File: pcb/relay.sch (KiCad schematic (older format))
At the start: 22 parts, among them IC1 ATTINY13-P, P1 CONN_01X02, P2 CONN_02X20, Q1 BC548, Q2 BC548, SW1 SW_PUSH, U1 78L05, U2 DX_MODULE

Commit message: More work on PCB
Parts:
- removed U1: 78L05, symbol 78L05
- added U1: MC78L05ACP, TO_SOT_Packages_THT:TO-92_Rugged, symbol MC78L05ACP
- C1: footprint (none) -> Capacitors_ThroughHole:C_Disc_D6_P5
- C2, C3: footprint (none) -> Capacitors_ThroughHole:C_Radial_D5_L11_P2.5
- D1: footprint (none) -> LEDs:LED-5MM
- D2, D3: footprint (none) -> Discret:D5
- IC1: footprint DIP8 -> Housings_DIP:DIP-8_W7.62mm_LongPads
- JP1: footprint (none) -> Pin_Headers:Pin_Header_Straight_1x02
- P1: footprint (none) -> Connect:bornier2
- P2: footprint (none) -> Connect:IDC_Header_Straight_40pins
- Q1, Q2: footprint TO-92 -> TO_SOT_Packages_THT:TO-92_Rugged
- R1, R2, R3, R4, R5: footprint (none) -> Resistors_ThroughHole:Resistor_Horizontal_RM10mm
- RL1, RL2: footprint (none) -> anritsu:anritsu
- SW1: footprint (none) -> Buttons_Switches_ThroughHole:SW_PUSH-12mm
- U2: footprint (none) -> dx_module:dx_module
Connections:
- net +12V: now also C2.1, P1.2 (P2), U1.3 (IN)
- net +5VD: now also U1.1 (OUT)
- net at C2.2, C3.2, P1.1 (P1): now also U1.2 (GND)
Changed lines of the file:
@@
 LIBS:anritsu
 LIBS:dx_module
+LIBS:relay-cache
 EELAYER 25 0
 EELAYER END
@@
 F 0 "IC1" H 1150 1850 50  0000 C CNN
 F 1 "ATTINY13-P" H 2600 1050 50  0000 C CNN
-F 2 "DIP8" H 2600 1450 50  0000 C CIN
+F 2 "Housings_DIP:DIP-8_W7.62mm_LongPads" H 2600 1450 50  0000 C CIN
 F 3 "" H 1150 1800 50  0000 C CNN
 	1    1950 1450
@@
 F 0 "Q1" H 5450 2025 50  0000 L CNN
 F 1 "BC548" H 5450 1950 50  0000 L CNN
-F 2 "TO-92" H 5450 1875 50  0000 L CIN
+F 2 "TO_SOT_Packages_THT:TO-92_Rugged" H 5450 1875 50  0000 L CIN
 F 3 "" H 5250 1950 50  0000 L CNN
 	1    5250 1950
@@
 F 0 "Q2" H 5450 4175 50  0000 L CNN
 F 1 "BC548" H 5450 4100 50  0000 L CNN
-F 2 "TO-92" H 5450 4025 50  0000 L CIN
+F 2 "TO_SOT_Packages_THT:TO-92_Rugged" H 5450 4025 50  0000 L CIN
 F 3 "" H 5250 4100 50  0000 L CNN
 	1    5250 4100
@@
 $EndComp
 $Comp
-L GNDD #PWR?
+L GNDD #PWR01
 U 1 1 57CD5BEB
 P 5350 2250
-F 0 "#PWR?" H 5350 2000 50  0001 C CNN
+F 0 "#PWR01" H 5350 2000 50  0001 C CNN
 F 1 "GNDD" H 5350 2100 50  0000 C CNN
 F 2 "" H 5350 2250 50  0000 C CNN
@@
 $EndComp
 $Comp
-L GNDD #PWR?
+L GNDD #PWR02
 U 1 1 57CD5C09
 P 950 1200
-F 0 "#PWR?" H 950 950 50  0001 C CNN
+F 0 "#PWR02" H 950 950 50  0001 C CNN
 F 1 "GNDD" H 950 1050 50  0000 C CNN
 F 2 "" H 950 1200 50  0000 C CNN
@@
 $EndComp
 $Comp
-L +5VD #PWR?
+L +5VD #PWR03
 U 1 1 57CD5C27
 P 950 1700
-F 0 "#PWR?" H 950 1550 50  0001 C CNN
+F 0 "#PWR03" H 950 1550 50  0001 C CNN
 F 1 "+5VD" H 950 1840 50  0000 C CNN
 F 2 "" H 950 1700 50  0000 C CNN
@@
 F 0 "D2" H 5350 1350 50  0000 C CNN
 F 1 "D" H 5350 1150 50  0000 C CNN
-F 2 "" H 5350 1250 50  0000 C CNN
+F 2 "Discret:D5" H 5350 1250 50  0000 C CNN
 F 3 "" H 5350 1250 50  0000 C CNN
 	1    5350 1250
@@
 F 0 "D3" H 5350 3450 50  0000 C CNN
 F 1 "D" H 5350 3250 50  0000 C CNN
-F 2 "" H 5350 3350 50  0000 C CNN
+F 2 "Discret:D5" H 5350 3350 50  0000 C CNN
 F 3 "" H 5350 3350 50  0000 C CNN
 	1    5350 3350
@@
 F 0 "R4" V 4980 1600 50  0000 C CNN
 F 1 "5K6" V 4900 1600 50  0000 C CNN
-F 2 "" V 4830 1600 50  0000 C CNN
+F 2 "Resistors_ThroughHole:Resistor_Horizontal_RM10mm" V 4830 1600 50  0000 C CNN
 F 3 "" H 4900 1600 50  0000 C CNN
 	1    4900 1600
@@
 F 0 "R5" V 4880 3500 50  0000 C CNN
 F 1 "5K6" V 4800 3500 50  0000 C CNN
-F 2 "" V 4730 3500 50  0000 C CNN
+F 2 "Resistors_ThroughHole:Resistor_Horizontal_RM10mm" V 4730 3500 50  0000 C CNN
 F 3 "" H 4800 3500 50  0000 C CNN
 	1    4800 3500
@@
 F 0 "R2" V 4530 1850 50  0000 C CNN
 F 1 "1M" V 4450 1850 50  0000 C CNN
-F 2 "" V 4380 1850 50  0000 C CNN
+F 2 "Resistors_ThroughHole:Resistor_Horizontal_RM10mm" V 4380 1850 50  0000 C CNN
 F 3 "" H 4450 1850 50  0000 C CNN
 	1    4450 1850
@@
 F 0 "R3" V 4530 2250 50  0000 C CNN
 F 1 "330K" V 4450 2250 50  0000 C CNN
-F 2 "" V 4380 2250 50  0000 C CNN
+F 2 "Resistors_ThroughHole:Resistor_Horizontal_RM10mm" V 4380 2250 50  0000 C CNN
 F 3 "" H 4450 2250 50  0000 C CNN
 	1    4450 2250
@@
 $EndComp
 $Comp
-L +12V #PWR?
+L +12V #PWR04
 U 1 1 57CD66EF
 P 4450 1700
-F 0 "#PWR?" H 4450 1550 50  0001 C CNN
+F 0 "#PWR04" H 4450 1550 50  0001 C CNN
 F 1 "+12V" H 4450 1840 50  0000 C CNN
 F 2 "" H 4450 1700 50  0000 C CNN
@@
 F 0 "C1" H 4225 2350 50  0000 L CNN
 F 1 "C" H 4225 2150 50  0000 L CNN
-F 2 "" H 4238 2100 50  0000 C CNN
+F 2 "Capacitors_ThroughHole:C_Disc_D6_P5" H 4238 2100 50  0000 C CNN
 F 3 "" H 4200 2250 50  0000 C CNN
 	1    4200 2250
@@
 $EndComp
 $Comp
-L GNDD #PWR?
+L GNDD #PWR05
 U 1 1 57CD68E3
 P 4450 2500
-F 0 "#PWR?" H 4450 2250 50  0001 C CNN
+F 0 "#PWR05" H 4450 2250 50  0001 C CNN
 F 1 "GNDD" H 4450 2350 50  0000 C CNN
 F 2 "" H 4450 2500 50  0000 C CNN
@@
 F 0 "P1" H 1250 5150 50  0000 C CNN
 F 1 "CONN_01X02" V 1350 5000 50  0000 C CNN
-F 2 "" H 1250 5000 50  0000 C CNN
+F 2 "Connect:bornier2" H 1250 5000 50  0000 C CNN
 F 3 "" H 1250 5000 50  0000 C CNN
 	1    1250 5000
@@
 F 0 "C2" H 2275 5300 50  0000 L CNN
 F 1 "1uF" H 2275 5100 50  0000 L CNN
-F 2 "" H 2288 5050 50  0000 C CNN
+F 2 "Capacitors_ThroughHole:C_Radial_D5_L11_P2.5" H 2288 5050 50  0000 C CNN
 F 3 "" H 2250 5200 50  0000 C CNN
 	1    2250 5200
@@
 F 0 "C3" H 3375 5300 50  0000 L CNN
 F 1 "1uF" H 3375 5100 50  0000 L CNN
-F 2 "" H 3388 5050 50  0000 C CNN
+F 2 "Capacitors_ThroughHole:C_Radial_D5_L11_P2.5" H 3388 5050 50  0000 C CNN
 F 3 "" H 3350 5200 50  0000 C CNN
 	1    3350 5200
@@
 $EndComp
 $Comp
-L 78L05 U1
-U 1 1 57CD72E7
-P 2850 5000
-F 0 "U1" H 3000 4804 50  0000 C CNN
-F 1 "78L05" H 2850 5200 50  0000 C CNN
-F 2 "" H 2850 5000 50  0000 C CNN
-F 3 "" H 2850 5000 50  0000 C CNN
-	1    2850 5000
-	1    0    0    -1
-$EndComp
-$Comp
-L +5VD #PWR?
+L +5VD #PWR06
 U 1 1 57CD74DA
 P 3350 4950
-F 0 "#PWR?" H 3350 4800 50  0001 C CNN
+F 0 "#PWR06" H 3350 4800 50  0001 C CNN
 F 1 "+5VD" H 3350 5090 50  0000 C CNN
 F 2 "" H 3350 4950 50  0000 C CNN
@@
 $EndComp
 $Comp
-L +12V #PWR?
+L +12V #PWR07
 U 1 1 57CD7D1E
-P 1650 4950
-F 0 "#PWR?" H 1650 4800 50  0001 C CNN
-F 1 "+12V" H 1650 5090 50  0000 C CNN
-F 2 "" H 1650 4950 50  0000 C CNN
-F 3 "" H 1650 4950 50  0000 C CNN
-	1    1650 4950
+P 2250 4950
+F 0 "#PWR07" H 2250 4800 50  0001 C CNN
+F 1 "+12V" H 2250 5090 50  0000 C CNN
+F 2 "" H 2250 4950 50  0000 C CNN
+F 3 "" H 2250 4950 50  0000 C CNN
+	1    2250 4950
 	1    0    0    -1
 $EndComp
@@
 F 0 "R1" V 3880 1800 50  0000 C CNN
 F 1 "1K" V 3800 1800 50  0000 C CNN
-F 2 "" V 3730 1800 50  0000 C CNN
+F 2 "Resistors_ThroughHole:Resistor_Horizontal_RM10mm" V 3730 1800 50  0000 C CNN
 F 3 "" H 3800 1800 50  0000 C CNN
 	1    3800 1800
@@
 F 0 "D1" H 3800 2300 50  0000 C CNN
 F 1 "LED" H 3800 2100 50  0000 C CNN
-F 2 "" H 3800 2200 50  0000 C CNN
+F 2 "LEDs:LED-5MM" H 3800 2200 50  0000 C CNN
 F 3 "" H 3800 2200 50  0000 C CNN
 	1    3800 2200
@@
 F 0 "SW1" H 3550 2160 50  0000 C CNN
 F 1 "SW_PUSH" H 3400 1970 50  0000 C CNN
-F 2 "" H 3400 2050 50  0000 C CNN
+F 2 "Buttons_Switches_ThroughHole:SW_PUSH-12mm" H 3400 2050 50  0000 C CNN
 F 3 "" H 3400 2050 50  0000 C CNN
 	1    3400 2050
@@
 F 0 "P2" H 10050 3250 50  0000 C CNN
 F 1 "CONN_02X20" V 10050 2200 50  0000 C CNN
-F 2 "" H 10050 1250 50  0000 C CNN
+F 2 "Connect:IDC_Header_Straight_40pins" H 10050 1250 50  0000 C CNN
 F 3 "" H 10050 1250 50  0000 C CNN
 	1    10050 2200
@@
 $EndComp
 $Comp
-L +12V #PWR?
+L +12V #PWR08
 U 1 1 57CD90B3
 P 6000 2850
-F 0 "#PWR?" H 6000 2700 50  0001 C CNN
+F 0 "#PWR08" H 6000 2700 50  0001 C CNN
 F 1 "+12V" H 6000 2990 50  0000 C CNN
 F 2 "" H 6000 2850 50  0000 C CNN
@@
 $EndComp
 $Comp
-L +12V #PWR?
+L +12V #PWR09
 U 1 1 57CD90EF
 P 6000 750
-F 0 "#PWR?" H 6000 600 50  0001 C CNN
+F 0 "#PWR09" H 6000 600 50  0001 C CNN
 F 1 "+12V" H 6000 890 50  0000 C CNN
 F 2 "" H 6000 750 50  0000 C CNN
@@
 $EndComp
 $Comp
-L GNDD #PWR?
+L GNDD #PWR010
 U 1 1 57CD9222
 P 5350 4350
-F 0 "#PWR?" H 5350 4100 50  0001 C CNN
+F 0 "#PWR010" H 5350 4100 50  0001 C CNN
 F 1 "GNDD" H 5350 4200 50  0000 C CNN
 F 2 "" H 5350 4350 50  0000 C CNN
@@
 F 0 "RL1" H 7050 1350 50  0000 L CNN
 F 1 "Anritsu" H 7050 1250 50  0000 L CNN
-F 2 "" H 6200 1200 50  0000 C CNN
+F 2 "anritsu:anritsu" H 6200 1200 50  0000 C CNN
 F 3 "" H 6200 1200 50  0000 C CNN
 	1    6200 1200
@@
 F 0 "RL2" H 7050 3450 50  0000 L CNN
 F 1 "Anritsu" H 7050 3350 50  0000 L CNN
-F 2 "" H 6200 3300 50  0000 C CNN
+F 2 "anritsu:anritsu" H 6200 3300 50  0000 C CNN
 F 3 "" H 6200 3300 50  0000 C CNN
 	1    6200 3300
@@
 F 0 "U2" H 8900 1900 60  0000 C CNN
 F 1 "DX_MODULE" H 8100 1900 60  0000 C CNN
-F 2 "" H 8400 1450 60  0001 C CNN
+F 2 "dx_module:dx_module" H 8400 1450 60  0001 C CNN
 F 3 "" H 8400 1450 60  0001 C CNN
 	1    8400 1450
@@
 F 0 "JP1" H 8400 2800 50  0000 C CNN
 F 1 "JUMPER" H 8400 2570 50  0000 C CNN
-F 2 "" H 8400 2650 50  0000 C CNN
+F 2 "Pin_Headers:Pin_Header_Straight_1x02" H 8400 2650 50  0000 C CNN
 F 3 "" H 8400 2650 50  0000 C CNN
 	1    8400 2650
@@
 Wire Wire Line
 	9400 1750 9800 1750
+$Comp
+L MC78L05ACP U1
+U 1 1 57D0150E
+P 2850 5000
+F 0 "U1" V 2650 5200 50  0000 C CNN
+F 1 "MC78L05ACP" H 2850 5200 50  0000 L CNN
+F 2 "TO_SOT_Packages_THT:TO-92_Rugged" H 2850 5100 50  0000 C CIN
+F 3 "" H 2850 5000 50  0000 C CNN
+	1    2850 5000
+	1    0    0    -1
+$EndComp
 $EndSCHEMATC

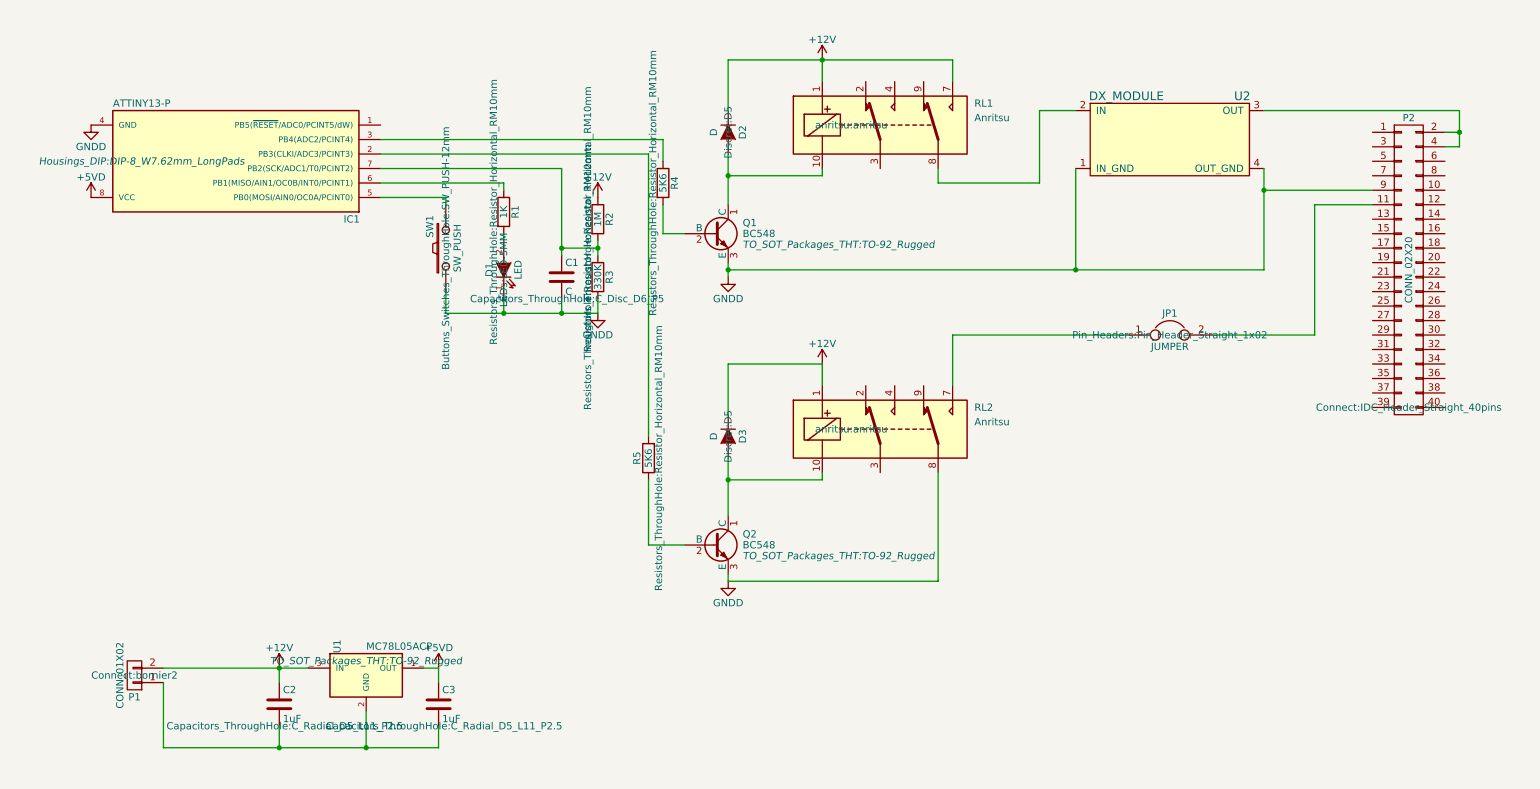
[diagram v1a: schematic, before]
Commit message: Changed footprints on PCB.
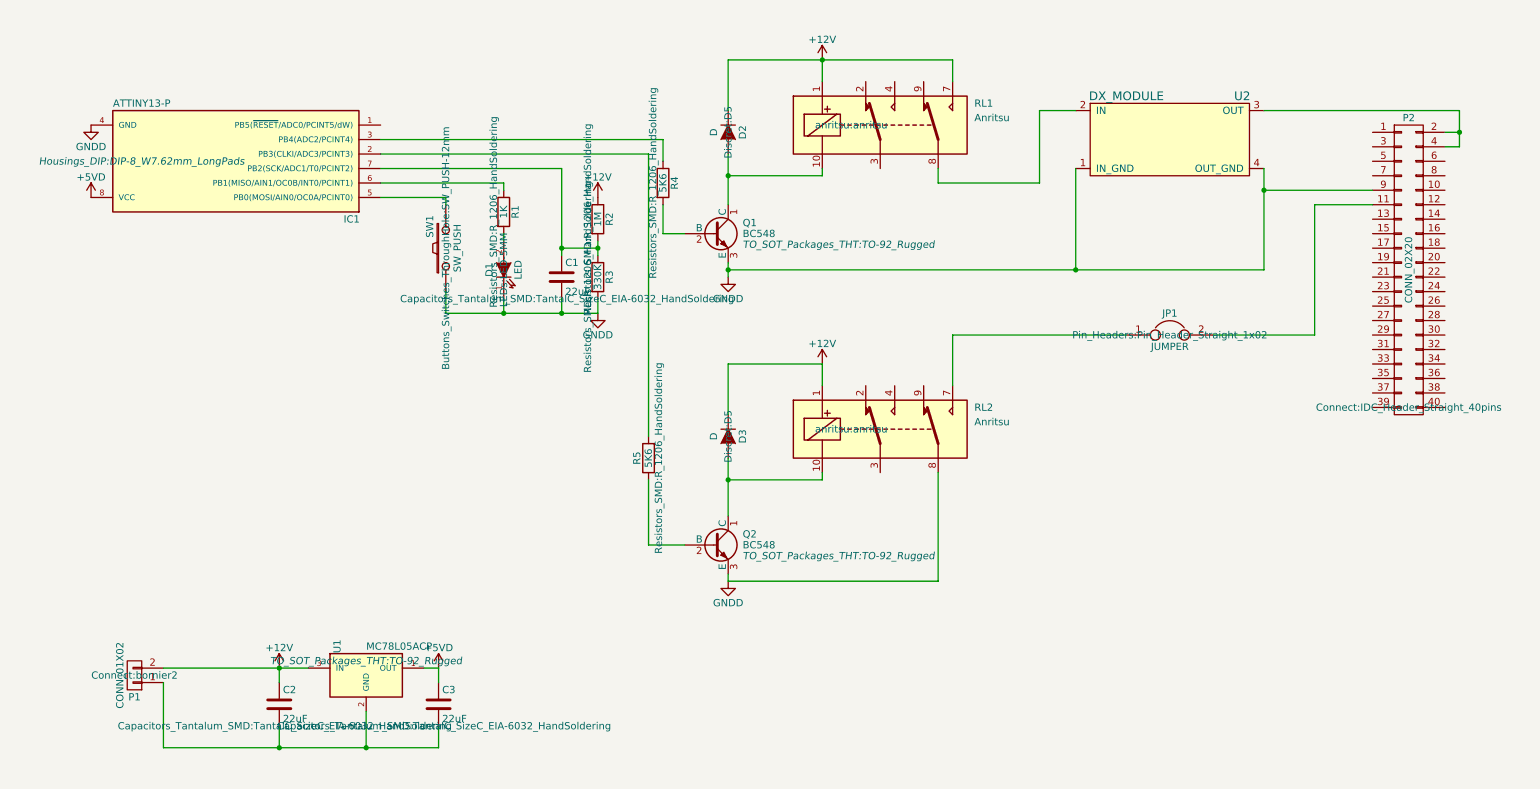
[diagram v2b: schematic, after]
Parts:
- C1: value C -> 22uF; footprint Capacitors_ThroughHole:C_Disc_D6_P5 -> Capacitors_Tantalum_SMD:TantalC_SizeC_EIA-6032_HandSoldering
- C2, C3: value 1uF -> 22uF; footprint Capacitors_ThroughHole:C_Radial_D5_L11_P2.5 -> Capacitors_Tantalum_SMD:TantalC_SizeC_EIA-6032_HandSoldering
- R1, R2, R3, R4, R5: footprint Resistors_ThroughHole:Resistor_Horizontal_RM10mm -> Resistors_SMD:R_1206_HandSoldering
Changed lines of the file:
@@
 F 0 "R4" V 4980 1600 50  0000 C CNN
 F 1 "5K6" V 4900 1600 50  0000 C CNN
-F 2 "Resistors_ThroughHole:Resistor_Horizontal_RM10mm" V 4830 1600 50  0000 C CNN
+F 2 "Resistors_SMD:R_1206_HandSoldering" V 4830 1600 50  0000 C CNN
 F 3 "" H 4900 1600 50  0000 C CNN
 	1    4900 1600
@@
 F 0 "R5" V 4880 3500 50  0000 C CNN
 F 1 "5K6" V 4800 3500 50  0000 C CNN
-F 2 "Resistors_ThroughHole:Resistor_Horizontal_RM10mm" V 4730 3500 50  0000 C CNN
+F 2 "Resistors_SMD:R_1206_HandSoldering" V 4730 3500 50  0000 C CNN
 F 3 "" H 4800 3500 50  0000 C CNN
 	1    4800 3500
@@
 F 0 "R2" V 4530 1850 50  0000 C CNN
 F 1 "1M" V 4450 1850 50  0000 C CNN
-F 2 "Resistors_ThroughHole:Resistor_Horizontal_RM10mm" V 4380 1850 50  0000 C CNN
+F 2 "Resistors_SMD:R_1206_HandSoldering" V 4380 1850 50  0000 C CNN
 F 3 "" H 4450 1850 50  0000 C CNN
 	1    4450 1850
@@
 F 0 "R3" V 4530 2250 50  0000 C CNN
 F 1 "330K" V 4450 2250 50  0000 C CNN
-F 2 "Resistors_ThroughHole:Resistor_Horizontal_RM10mm" V 4380 2250 50  0000 C CNN
+F 2 "Resistors_SMD:R_1206_HandSoldering" V 4380 2250 50  0000 C CNN
 F 3 "" H 4450 2250 50  0000 C CNN
 	1    4450 2250
@@
 P 4200 2250
 F 0 "C1" H 4225 2350 50  0000 L CNN
-F 1 "C" H 4225 2150 50  0000 L CNN
-F 2 "Capacitors_ThroughHole:C_Disc_D6_P5" H 4238 2100 50  0000 C CNN
+F 1 "22uF" H 4225 2150 50  0000 L CNN
+F 2 "Capacitors_Tantalum_SMD:TantalC_SizeC_EIA-6032_HandSoldering" H 4238 2100 50  0000 C CNN
 F 3 "" H 4200 2250 50  0000 C CNN
 	1    4200 2250
@@
 P 2250 5200
 F 0 "C2" H 2275 5300 50  0000 L CNN
-F 1 "1uF" H 2275 5100 50  0000 L CNN
-F 2 "Capacitors_ThroughHole:C_Radial_D5_L11_P2.5" H 2288 5050 50  0000 C CNN
+F 1 "22uF" H 2275 5100 50  0000 L CNN
+F 2 "Capacitors_Tantalum_SMD:TantalC_SizeC_EIA-6032_HandSoldering" H 2288 5050 50  0000 C CNN
 F 3 "" H 2250 5200 50  0000 C CNN
 	1    2250 5200
@@
 P 3350 5200
 F 0 "C3" H 3375 5300 50  0000 L CNN
-F 1 "1uF" H 3375 5100 50  0000 L CNN
-F 2 "Capacitors_ThroughHole:C_Radial_D5_L11_P2.5" H 3388 5050 50  0000 C CNN
+F 1 "22uF" H 3375 5100 50  0000 L CNN
+F 2 "Capacitors_Tantalum_SMD:TantalC_SizeC_EIA-6032_HandSoldering" H 3388 5050 50  0000 C CNN
 F 3 "" H 3350 5200 50  0000 C CNN
 	1    3350 5200
@@
 F 0 "R1" V 3880 1800 50  0000 C CNN
 F 1 "1K" V 3800 1800 50  0000 C CNN
-F 2 "Resistors_ThroughHole:Resistor_Horizontal_RM10mm" V 3730 1800 50  0000 C CNN
+F 2 "Resistors_SMD:R_1206_HandSoldering" V 3730 1800 50  0000 C CNN
 F 3 "" H 3800 1800 50  0000 C CNN
 	1    3800 1800

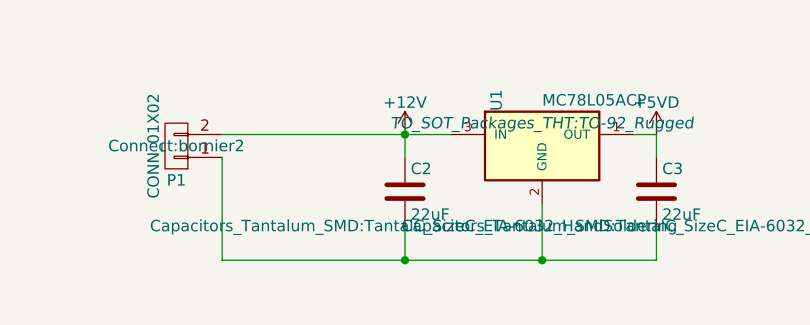
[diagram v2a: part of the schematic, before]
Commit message: Final version of PCB sent to OSHPark.
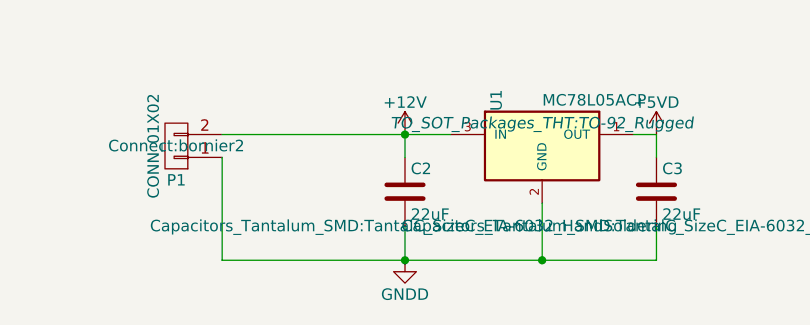
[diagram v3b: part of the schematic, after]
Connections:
- net GNDD: now also C2.2, C3.2, P1.1 (P1), U1.2 (GND)
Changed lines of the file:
@@
+	1    0    0    -1
+$EndComp
+$Comp
+L GNDD #PWR?
+U 1 1 57D16765
+P 2250 5500
+F 0 "#PWR?" H 2250 5250 50  0001 C CNN
+F 1 "GNDD" H 2250 5350 50  0000 C CNN
+F 2 "" H 2250 5500 50  0000 C CNN
+F 3 "" H 2250 5500 50  0000 C CNN
+	1    2250 5500
 	1    0    0    -1
 $EndComp
